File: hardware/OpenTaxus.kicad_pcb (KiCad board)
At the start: 2 copper layers, 66.7 x 85.7 mm, 54 parts, among them J1 OLED, J2 qwiic, J3 SWD, J4 USB_C_Receptacle_USB2.0, Q2 BC847BS, Q3 PT12-21B/TR8, SW1 dpad, SW2 USB_BOOT, SW3 RESET, SW4 SW_SPDT, U1 HE6206-33NR, U2 W25Q128JVS, U3 RP2040, U4 XT1861B332MR-G, Y1 YSX321SL

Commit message: adding bsidespdx logo to badge
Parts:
- added REF**: bsidespdx, logos:bsidespdx, B.Cu at (59.0, 28.7)
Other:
- board text added: "github.com/pdxbadgers/badge-2024"
- board text removed: "github.com/securelyfitz/opentaxus"
- board text removed: "↑ trade ↔ info ↓ sleep"

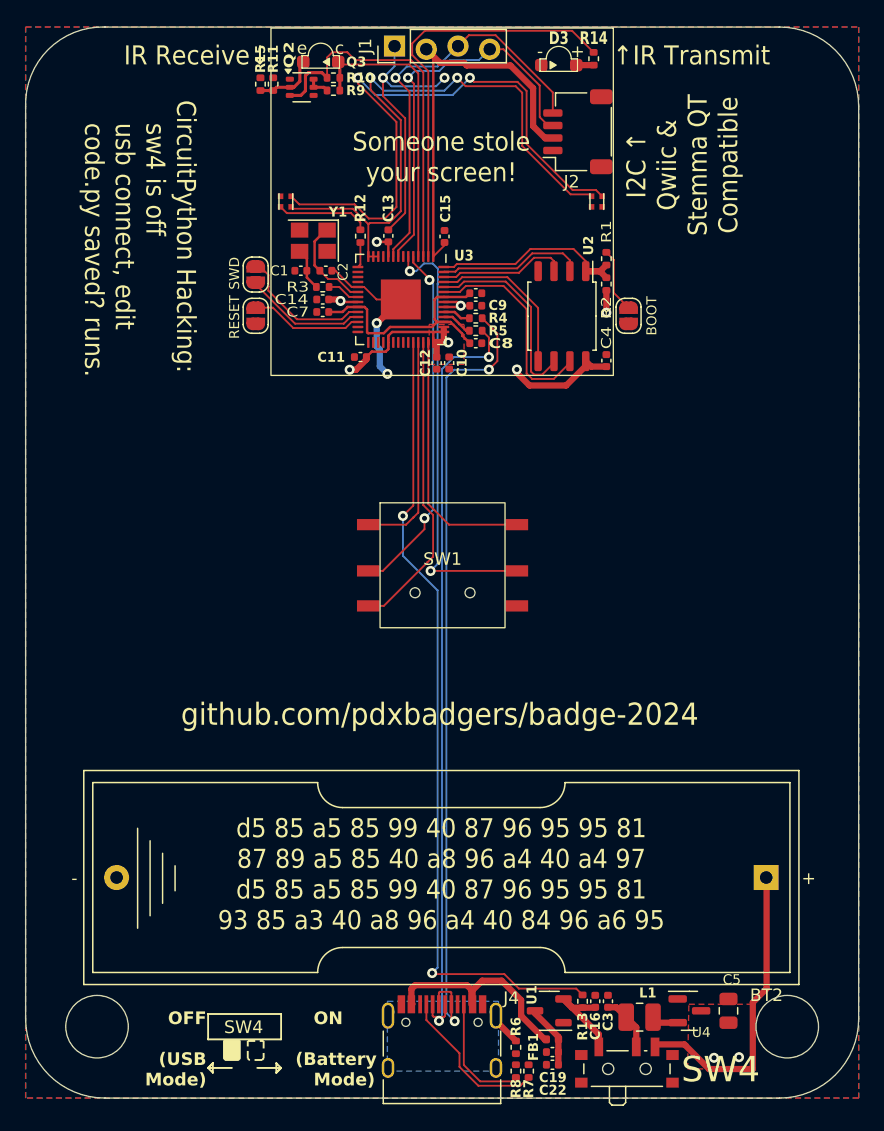
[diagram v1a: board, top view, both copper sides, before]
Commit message: fine tune via locaions to be hidden by black soldermask
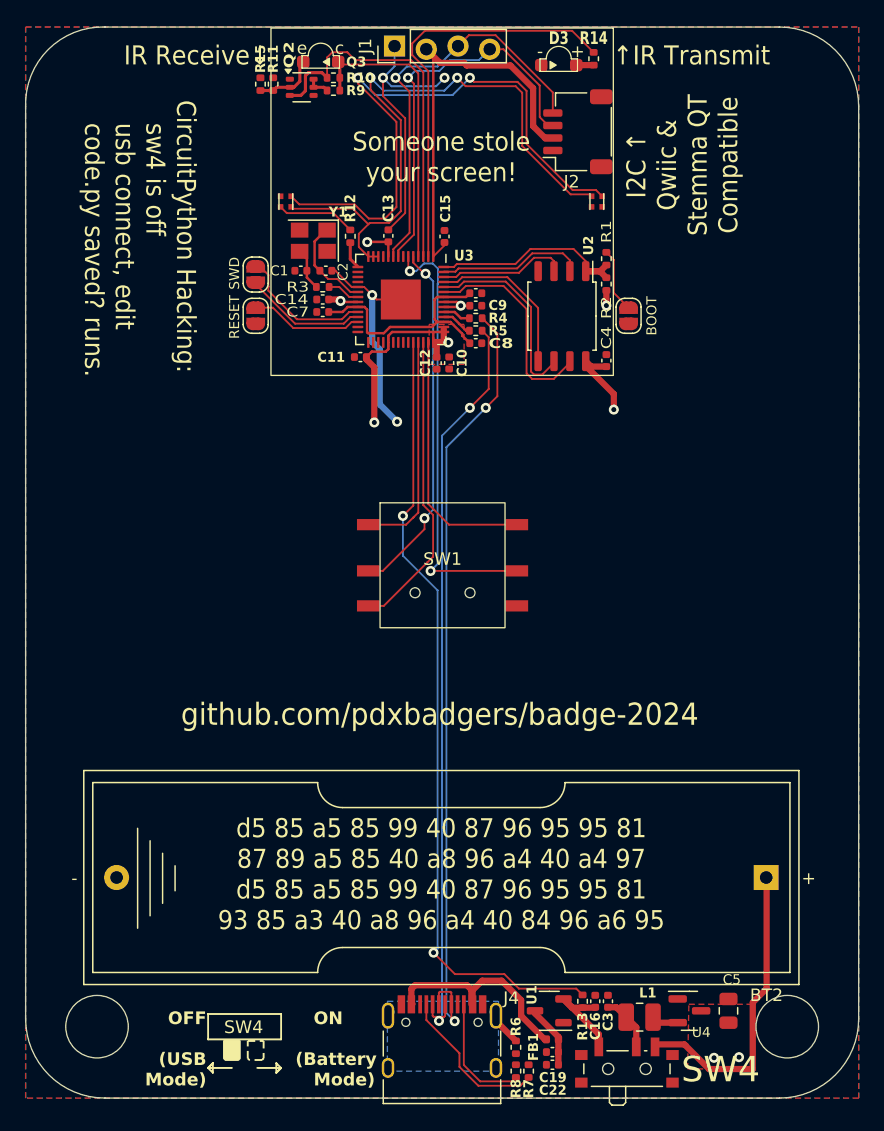
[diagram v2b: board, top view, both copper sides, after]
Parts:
- R11: value 1k -> 5k1
- R14: value 220 -> 0
- moved R12 0.81 mm to (51.4, 42.2)
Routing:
- net GND: track 40.0 -> 43.8 mm
- net /USB_D-: track 62.0 -> 60.3 mm
- net /USB_D+: track 64.9 -> 63.3 mm
- net +3V3: track 65.9 -> 67.3 mm
- net Net-(D1-DIN): track 7.49 -> 6.35 mm
- net /GPIO26_ADC0/USB_DET: track 64.9 -> 63.8 mm
- net /GPIO11/NEO_PWR: track 50.1 -> 50.8 mm
